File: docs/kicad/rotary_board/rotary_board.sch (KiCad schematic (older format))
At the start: 8 parts

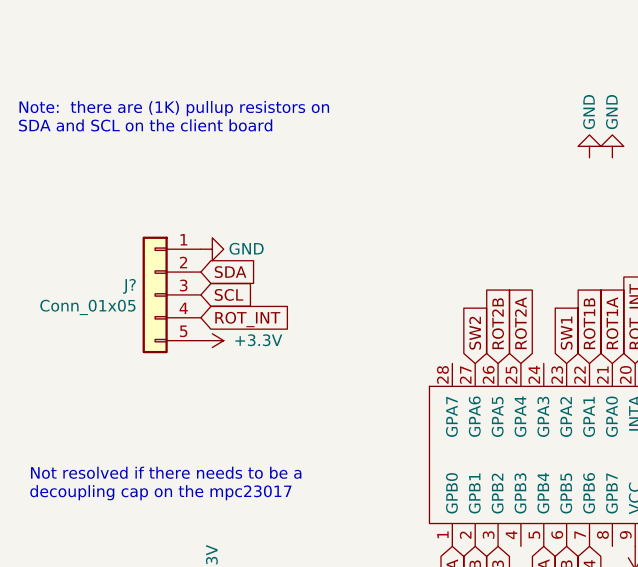
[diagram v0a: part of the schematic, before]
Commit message: got rid of (many) vestigial TE3 design attempts; consolidating electronics under TE3/docs/kicad
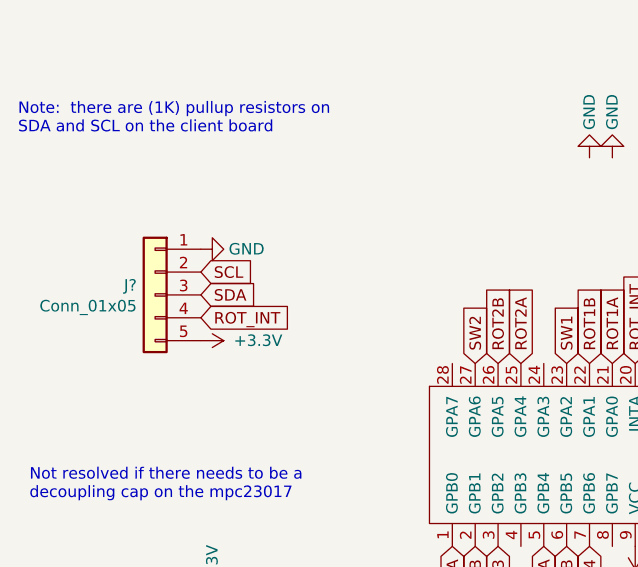
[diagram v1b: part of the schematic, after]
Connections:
- net SCL: now also J?.2 (Pin_2); no longer J?.3 (Pin_3)
- net SDA: now also J?.3 (Pin_3); no longer J?.2 (Pin_2)
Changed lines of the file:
@@
 Text GLabel 5050 3100 3    50   Input ~ 0
 SDA
+Text GLabel 2750 1900 2    50   Input ~ 0
+SCL
 Text GLabel 2750 2000 2    50   Input ~ 0
-SCL
-Text GLabel 2750 1900 2    50   Input ~ 0
 SDA
 Text GLabel 4650 2300 1    50   Input ~ 0

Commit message: tested prototype rotary board
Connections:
- net GND: now also U?.24 (GPA3), U?.28 (GPA7), U?.4 (GPB3), U?.8 (GPB7)
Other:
- note added: "Note: there are (1K) pullup resistors on\nSDA and SCL on the mother_board"
- note removed: "Note: there are (1K) pullup resistors on\nSDA and SCL on the client board"
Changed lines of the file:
@@
 L Device:C C?
 U 1 1 6643CD42
-P 2800 3600
-F 0 "C?" H 2915 3646 50  0001 L CNN
-F 1 "100nf" H 2915 3600 50  0000 L CNN
-F 2 "" H 2838 3450 50  0001 C CNN
-F 3 "~" H 2800 3600 50  0001 C CNN
-	1    2800 3600
+P 2650 3600
+F 0 "C?" H 2765 3646 50  0001 L CNN
+F 1 "100nf" H 2765 3600 50  0000 L CNN
+F 2 "" H 2688 3450 50  0001 C CNN
+F 3 "~" H 2650 3600 50  0001 C CNN
+	1    2650 3600
 	1    0    0    -1
 $EndComp
@@
 L power:+3.3V #PWR?
 U 1 1 66443A19
-P 2800 3450
-F 0 "#PWR?" H 2800 3300 50  0001 C CNN
-F 1 "+3.3V" V 2800 3700 50  0000 C CNN
-F 2 "" H 2800 3450 50  0001 C CNN
-F 3 "" H 2800 3450 50  0001 C CNN
-	1    2800 3450
+P 2650 3450
+F 0 "#PWR?" H 2650 3300 50  0001 C CNN
+F 1 "+3.3V" V 2650 3700 50  0000 C CNN
+F 2 "" H 2650 3450 50  0001 C CNN
+F 3 "" H 2650 3450 50  0001 C CNN
+	1    2650 3450
 	1    0    0    -1
 $EndComp
@@
 L power:GND #PWR?
 U 1 1 66444811
-P 2800 3750
-F 0 "#PWR?" H 2800 3500 50  0001 C CNN
-F 1 "GND" V 2800 3550 50  0000 C CNN
-F 2 "" H 2800 3750 50  0001 C CNN
-F 3 "" H 2800 3750 50  0001 C CNN
-	1    2800 3750
+P 2650 3750
+F 0 "#PWR?" H 2650 3500 50  0001 C CNN
+F 1 "GND" V 2650 3550 50  0000 C CNN
+F 2 "" H 2650 3750 50  0001 C CNN
+F 3 "" H 2650 3750 50  0001 C CNN
+	1    2650 3750
 	1    0    0    -1
 $EndComp
@@
 SW4
 $Comp
-L power:GND #PWR?
-U 1 1 66491CF1
-P 4600 3700
-F 0 "#PWR?" H 4600 3450 50  0001 C CNN
-F 1 "GND" V 4600 3500 50  0000 C CNN
-F 2 "" H 4600 3700 50  0001 C CNN
-F 3 "" H 4600 3700 50  0001 C CNN
-	1    4600 3700
-	1    0    0    -1
-$EndComp
-$Comp
-L power:GND #PWR?
-U 1 1 66491F00
-P 4700 3700
-F 0 "#PWR?" H 4700 3450 50  0001 C CNN
-F 1 "GND" V 4700 3500 50  0000 C CNN
-F 2 "" H 4700 3700 50  0001 C CNN
-F 3 "" H 4700 3700 50  0001 C CNN
-	1    4700 3700
-	1    0    0    -1
-$EndComp
-$Comp
-L power:GND #PWR?
-U 1 1 66495A69
-P 4450 1400
-F 0 "#PWR?" H 4450 1150 50  0001 C CNN
-F 1 "GND" V 4450 1200 50  0000 C CNN
-F 2 "" H 4450 1400 50  0001 C CNN
-F 3 "" H 4450 1400 50  0001 C CNN
-	1    4450 1400
-	-1   0    0    1
-$EndComp
-$Comp
-L power:GND #PWR?
-U 1 1 66495DD6
-P 4550 1400
-F 0 "#PWR?" H 4550 1150 50  0001 C CNN
-F 1 "GND" V 4550 1200 50  0000 C CNN
-F 2 "" H 4550 1400 50  0001 C CNN
-F 3 "" H 4550 1400 50  0001 C CNN
-	1    4550 1400
-	-1   0    0    1
-$EndComp
-$Comp
 L 0_my_symbols:mcp23017 U?
 U 1 1 663ECAFA
@@
 NoConn ~ 4750 2300
 Text Notes 1950 1300 0    50   ~ 0
-Note:  there are (1K) pullup resistors on\nSDA and SCL on the client board
+Note:  there are (1K) pullup resistors on\nSDA and SCL on the mother_board
 Text GLabel 4750 2300 1    50   Input ~ 0
 ROT_INT
@@
 Text Notes 5450 950  0    50   ~ 0
 may want 0.1uf ceramic caps tween pins and ground\nfor hardware debouncing
+$Comp
+L power:GND #PWR?
+U 1 1 66491F00
+P 4550 3100
+F 0 "#PWR?" H 4550 2850 50  0001 C CNN
+F 1 "GND" V 4550 2900 50  0000 C CNN
+F 2 "" H 4550 3100 50  0001 C CNN
+F 3 "" H 4550 3100 50  0001 C CNN
+	1    4550 3100
+	1    0    0    -1
+$EndComp
+$Comp
+L power:GND #PWR?
+U 1 1 66491CF1
+P 4150 3100
+F 0 "#PWR?" H 4150 2850 50  0001 C CNN
+F 1 "GND" V 4150 2900 50  0000 C CNN
+F 2 "" H 4150 3100 50  0001 C CNN
+F 3 "" H 4150 3100 50  0001 C CNN
+	1    4150 3100
+	1    0    0    -1
+$EndComp
+$Comp
+L power:GND #PWR?
+U 1 1 66495DD6
+P 4250 2300
+F 0 "#PWR?" H 4250 2050 50  0001 C CNN
+F 1 "GND" V 4250 2100 50  0000 C CNN
+F 2 "" H 4250 2300 50  0001 C CNN
+F 3 "" H 4250 2300 50  0001 C CNN
+	1    4250 2300
+	-1   0    0    1
+$EndComp
+$Comp
+L power:GND #PWR?
+U 1 1 66495A69
+P 3850 2300
+F 0 "#PWR?" H 3850 2050 50  0001 C CNN
+F 1 "GND" V 3850 2100 50  0000 C CNN
+F 2 "" H 3850 2300 50  0001 C CNN
+F 3 "" H 3850 2300 50  0001 C CNN
+	1    3850 2300
+	-1   0    0    1
+$EndComp
 $EndSCHEMATC

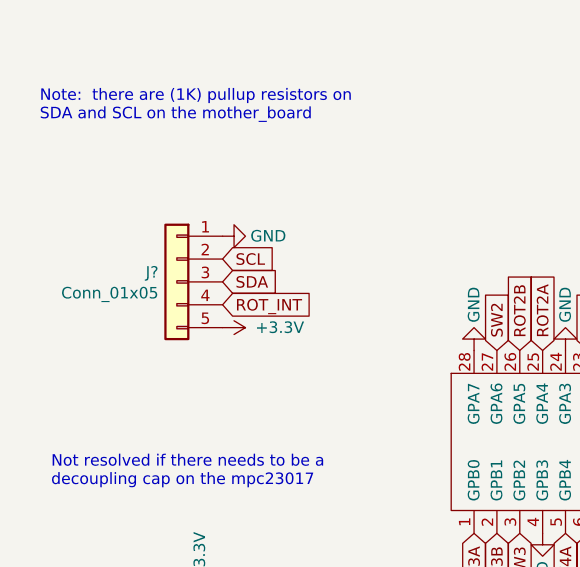
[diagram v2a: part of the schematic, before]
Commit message: kicad changes to support actual Fusion 360 TE3 design efforts - created rotary board PCB
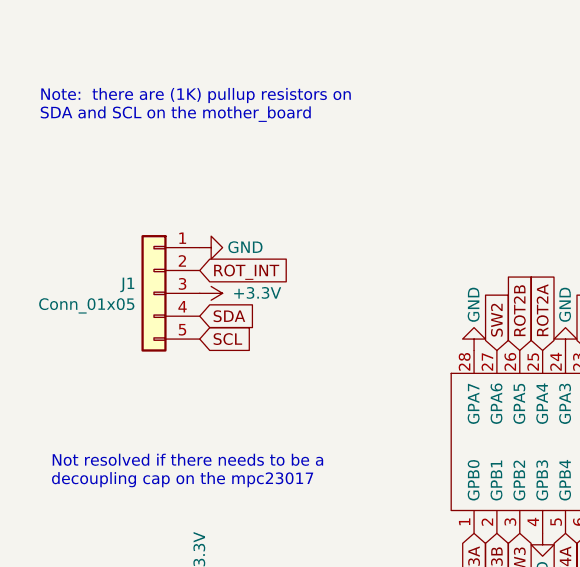
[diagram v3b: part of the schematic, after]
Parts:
- C1: renamed from C?; footprint (none) -> 0_my_footprints:myCapCeramicSmall
- J1: renamed from J?; footprint (none) -> 0_my_footprints:my5Pin
- R1: renamed from R?; footprint (none) -> 0_my_footprints:myResistor
- SW1, SW2, SW3, SW4: renamed from SW?; footprint (none) -> 0_my_footprints:myRotaryEncoder
- U1: renamed from U?; footprint (none) -> 0_my_footprints:myDip28
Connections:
- net +3V3: now also J1.3 (Pin_3); no longer J1.5 (Pin_5)
- net ROT_INT: now also J1.2 (Pin_2); no longer J1.4 (Pin_4)
- net SCL: now also J1.5 (Pin_5); no longer J1.2 (Pin_2)
- net SDA: now also J1.4 (Pin_4); no longer J1.3 (Pin_3)
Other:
- moved on the sheet: J1
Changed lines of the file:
@@
 $EndDescr
 $Comp
-L Device:Rotary_Encoder_Switch SW?
+L Device:Rotary_Encoder_Switch SW1
 U 1 1 663E57E0
 P 6500 1450
-F 0 "SW?" H 6500 1817 50  0001 C CNN
+F 0 "SW1" H 6500 1817 50  0001 C CNN
 F 1 "ROT1" H 6500 1725 50  0000 C CNN
-F 2 "" H 6350 1610 50  0001 C CNN
+F 2 "0_my_footprints:myRotaryEncoder" H 6350 1610 50  0001 C CNN
 F 3 "~" H 6500 1710 50  0001 C CNN
 	1    6500 1450
@@
 $EndComp
 $Comp
-L Connector_Generic:Conn_01x05 J?
+L Connector_Generic:Conn_01x05 J1
 U 1 1 663EE45D
-P 2550 2000
-F 0 "J?" H 2630 2042 50  0000 L CNN
-F 1 "Conn_01x05" H 2630 1951 50  0000 L CNN
-F 2 "" H 2550 2000 50  0001 C CNN
-F 3 "~" H 2550 2000 50  0001 C CNN
-	1    2550 2000
+P 2450 2050
+F 0 "J1" H 2530 2092 50  0000 L CNN
+F 1 "Conn_01x05" H 2530 2001 50  0000 L CNN
+F 2 "0_my_footprints:my5Pin" H 2450 2050 50  0001 C CNN
+F 3 "~" H 2450 2050 50  0001 C CNN
+	1    2450 2050
 	-1   0    0    -1
 $EndComp
 $Comp
-L Device:Rotary_Encoder_Switch SW?
+L Device:Rotary_Encoder_Switch SW2
 U 1 1 663F3D60
 P 6500 2300
-F 0 "SW?" H 6500 2667 50  0001 C CNN
+F 0 "SW2" H 6500 2667 50  0001 C CNN
 F 1 "ROT2" H 6500 2575 50  0000 C CNN
-F 2 "" H 6350 2460 50  0001 C CNN
+F 2 "0_my_footprints:myRotaryEncoder" H 6350 2460 50  0001 C CNN
 F 3 "~" H 6500 2560 50  0001 C CNN
 	1    6500 2300
@@
 $EndComp
 $Comp
-L Device:Rotary_Encoder_Switch SW?
+L Device:Rotary_Encoder_Switch SW3
 U 1 1 663F4490
 P 6500 3150
-F 0 "SW?" H 6500 3517 50  0001 C CNN
+F 0 "SW3" H 6500 3517 50  0001 C CNN
 F 1 "ROT3" H 6500 3425 50  0000 C CNN
-F 2 "" H 6350 3310 50  0001 C CNN
+F 2 "0_my_footprints:myRotaryEncoder" H 6350 3310 50  0001 C CNN
 F 3 "~" H 6500 3410 50  0001 C CNN
 	1    6500 3150
@@
 $EndComp
 $Comp
-L Device:Rotary_Encoder_Switch SW?
+L Device:Rotary_Encoder_Switch SW4
 U 1 1 663F4B46
 P 6500 4050
-F 0 "SW?" H 6500 4417 50  0001 C CNN
+F 0 "SW4" H 6500 4417 50  0001 C CNN
 F 1 "ROT4" H 6500 4325 50  0000 C CNN
-F 2 "" H 6350 4210 50  0001 C CNN
+F 2 "0_my_footprints:myRotaryEncoder" H 6350 4210 50  0001 C CNN
 F 3 "~" H 6500 4310 50  0001 C CNN
 	1    6500 4050
@@
 $EndComp
 $Comp
-L power:GND #PWR?
+L power:GND #PWR03
 U 1 1 663F4E53
-P 2750 1800
-F 0 "#PWR?" H 2750 1550 50  0001 C CNN
-F 1 "GND" V 2750 1600 50  0000 C CNN
-F 2 "" H 2750 1800 50  0001 C CNN
-F 3 "" H 2750 1800 50  0001 C CNN
-	1    2750 1800
-	0    -1   -1   0
-$EndComp
-$Comp
-L power:GND #PWR?
+P 2650 1850
+F 0 "#PWR03" H 2650 1600 50  0001 C CNN
+F 1 "GND" V 2650 1650 50  0000 C CNN
+F 2 "" H 2650 1850 50  0001 C CNN
+F 3 "" H 2650 1850 50  0001 C CNN
+	1    2650 1850
+	0    -1   1    0
+$EndComp
+$Comp
+L power:GND #PWR016
 U 1 1 663F68D2
 P 4750 3100
-F 0 "#PWR?" H 4750 2850 50  0001 C CNN
+F 0 "#PWR016" H 4750 2850 50  0001 C CNN
 F 1 "GND" V 4750 2900 50  0000 C CNN
 F 2 "" H 4750 3100 50  0001 C CNN
@@
 $EndComp
 $Comp
-L power:+3.3V #PWR?
+L power:+3.3V #PWR05
 U 1 1 663F6C65
-P 2750 2200
-F 0 "#PWR?" H 2750 2050 50  0001 C CNN
-F 1 "+3.3V" V 2750 2450 50  0000 C CNN
-F 2 "" H 2750 2200 50  0001 C CNN
-F 3 "" H 2750 2200 50  0001 C CNN
-	1    2750 2200
-	0    1    1    0
+P 2650 2050
+F 0 "#PWR05" H 2650 1900 50  0001 C CNN
+F 1 "+3.3V" V 2650 2300 50  0000 C CNN
+F 2 "" H 2650 2050 50  0001 C CNN
+F 3 "" H 2650 2050 50  0001 C CNN
+	1    2650 2050
+	0    1    -1   0
 $EndComp
 Text GLabel 6800 1350 2    50   Input ~ 0
@@
 ROT4B
 $Comp
-L power:GND #PWR?
+L power:GND #PWR012
 U 1 1 664272DF
 P 6800 2400
-F 0 "#PWR?" H 6800 2150 50  0001 C CNN
+F 0 "#PWR012" H 6800 2150 50  0001 C CNN
 F 1 "GND" V 6800 2200 50  0000 C CNN
 F 2 "" H 6800 2400 50  0001 C CNN
@@
 $EndComp
 $Comp
-L power:GND #PWR?
+L power:GND #PWR020
 U 1 1 66427662
 P 6800 3250
-F 0 "#PWR?" H 6800 3000 50  0001 C CNN
+F 0 "#PWR020" H 6800 3000 50  0001 C CNN
 F 1 "GND" V 6800 3050 50  0000 C CNN
 F 2 "" H 6800 3250 50  0001 C CNN
@@
 $EndComp
 $Comp
-L power:GND #PWR?
+L power:GND #PWR024
 U 1 1 66427948
 P 6800 4150
-F 0 "#PWR?" H 6800 3900 50  0001 C CNN
+F 0 "#PWR024" H 6800 3900 50  0001 C CNN
 F 1 "GND" V 6800 3950 50  0000 C CNN
 F 2 "" H 6800 4150 50  0001 C CNN
@@
 $EndComp
 $Comp
-L power:GND #PWR?
+L power:GND #PWR02
 U 1 1 66428D78
 P 6800 1550
-F 0 "#PWR?" H 6800 1300 50  0001 C CNN
+F 0 "#PWR02" H 6800 1300 50  0001 C CNN
 F 1 "GND" V 6800 1350 50  0000 C CNN
 F 2 "" H 6800 1550 50  0001 C CNN
@@
 $EndComp
 $Comp
-L power:GND #PWR?
+L power:GND #PWR01
 U 1 1 66429552
 P 6200 1450
-F 0 "#PWR?" H 6200 1200 50  0001 C CNN
+F 0 "#PWR01" H 6200 1200 50  0001 C CNN
 F 1 "GND" V 6200 1250 50  0000 C CNN
 F 2 "" H 6200 1450 50  0001 C CNN
@@
 $EndComp
 $Comp
-L power:GND #PWR?
+L power:GND #PWR011
 U 1 1 66429883
 P 6200 2300
-F 0 "#PWR?" H 6200 2050 50  0001 C CNN
+F 0 "#PWR011" H 6200 2050 50  0001 C CNN
 F 1 "GND" V 6200 2100 50  0000 C CNN
 F 2 "" H 6200 2300 50  0001 C CNN
@@
 $EndComp
 $Comp
-L power:GND #PWR?
+L power:GND #PWR019
 U 1 1 6642A07A
 P 6200 3150
-F 0 "#PWR?" H 6200 2900 50  0001 C CNN
+F 0 "#PWR019" H 6200 2900 50  0001 C CNN
 F 1 "GND" V 6200 2950 50  0000 C CNN
 F 2 "" H 6200 3150 50  0001 C CNN
@@
 $EndComp
 $Comp
-L power:GND #PWR?
+L power:GND #PWR023
 U 1 1 6642A3A3
 P 6200 4050
-F 0 "#PWR?" H 6200 3800 50  0001 C CNN
+F 0 "#PWR023" H 6200 3800 50  0001 C CNN
 F 1 "GND" V 6200 3850 50  0000 C CNN
 F 2 "" H 6200 4050 50  0001 C CNN
@@
 $EndComp
 $Comp
-L power:+3.3V #PWR?
+L power:+3.3V #PWR015
 U 1 1 6643C635
 P 4650 3100
-F 0 "#PWR?" H 4650 2950 50  0001 C CNN
+F 0 "#PWR015" H 4650 2950 50  0001 C CNN
 F 1 "+3.3V" V 4650 3350 50  0000 C CNN
 F 2 "" H 4650 3100 50  0001 C CNN
@@
 $EndComp
 $Comp
-L Device:R R?
+L Device:R R1
 U 1 1 6643CB12
 P 4850 2050
-F 0 "R?" H 4920 2096 50  0001 L CNN
+F 0 "R1" H 4920 2096 50  0001 L CNN
 F 1 "10K" V 4850 2050 50  0000 C CNN
-F 2 "" V 4780 2050 50  0001 C CNN
+F 2 "0_my_footprints:myResistor" V 4780 2050 50  0001 C CNN
 F 3 "~" H 4850 2050 50  0001 C CNN
 	1    4850 2050
@@
 $EndComp
 $Comp
-L Device:C C?
+L Device:C C1
 U 1 1 6643CD42
 P 2650 3600
-F 0 "C?" H 2765 3646 50  0001 L CNN
+F 0 "C1" H 2765 3646 50  0001 L CNN
 F 1 "100nf" H 2765 3600 50  0000 L CNN
-F 2 "" H 2688 3450 50  0001 C CNN
+F 2 "0_my_footprints:myCapCeramicSmall" H 2688 3450 50  0001 C CNN
 F 3 "~" H 2650 3600 50  0001 C CNN
 	1    2650 3600
@@
 $EndComp
 $Comp
-L power:+3.3V #PWR?
+L power:+3.3V #PWR021
 U 1 1 66443A19
 P 2650 3450
-F 0 "#PWR?" H 2650 3300 50  0001 C CNN
+F 0 "#PWR021" H 2650 3300 50  0001 C CNN
 F 1 "+3.3V" V 2650 3700 50  0000 C CNN
 F 2 "" H 2650 3450 50  0001 C CNN
@@
 $EndComp
 $Comp
-L power:GND #PWR?
+L power:GND #PWR022
 U 1 1 66444811
 P 2650 3750
-F 0 "#PWR?" H 2650 3500 50  0001 C CNN
+F 0 "#PWR022" H 2650 3500 50  0001 C CNN
 F 1 "GND" V 2650 3550 50  0000 C CNN
 F 2 "" H 2650 3750 50  0001 C CNN
@@
 $EndComp
 $Comp
-L power:+3.3V #PWR?
+L power:+3.3V #PWR04
 U 1 1 664504D1
 P 4850 1800
-F 0 "#PWR?" H 4850 1650 50  0001 C CNN
+F 0 "#PWR04" H 4850 1650 50  0001 C CNN
 F 1 "+3.3V" V 4850 2050 50  0000 C CNN
 F 2 "" H 4850 1800 50  0001 C CNN
@@
 SW4
 $Comp
-L 0_my_symbols:mcp23017 U?
+L 0_my_symbols:mcp23017 U1
 U 1 1 663ECAFA
 P 4500 2700
-F 0 "U?" H 5228 2746 50  0001 L CNN
+F 0 "U1" H 5228 2746 50  0001 L CNN
 F 1 "mcp23017" H 4700 2700 50  0000 L CNN
-F 2 "" H 4750 2450 50  0001 C CNN
+F 2 "0_my_footprints:myDip28" H 4750 2450 50  0001 C CNN
 F 3 "" H 4750 2450 50  0001 C CNN
 	1    4500 2700
@@
 $EndComp
 $Comp
-L power:GND #PWR?
+L power:GND #PWR010
 U 1 1 66499F8B
 P 5150 2300
-F 0 "#PWR?" H 5150 2050 50  0001 C CNN
+F 0 "#PWR010" H 5150 2050 50  0001 C CNN
 F 1 "GND" V 5150 2100 50  0000 C CNN
 F 2 "" H 5150 2300 50  0001 C CNN
@@
 $EndComp
 $Comp
-L power:GND #PWR?
+L power:GND #PWR09
 U 1 1 6649A25F
 P 5050 2300
-F 0 "#PWR?" H 5050 2050 50  0001 C CNN
+F 0 "#PWR09" H 5050 2050 50  0001 C CNN
 F 1 "GND" V 5050 2100 50  0000 C CNN
 F 2 "" H 5050 2300 50  0001 C CNN
@@
 $EndComp
 $Comp
-L power:GND #PWR?
+L power:GND #PWR08
 U 1 1 6649A57A
 P 4950 2300
-F 0 "#PWR?" H 4950 2050 50  0001 C CNN
+F 0 "#PWR08" H 4950 2050 50  0001 C CNN
 F 1 "GND" V 4950 2100 50  0000 C CNN
 F 2 "" H 4950 2300 50  0001 C CNN
@@
 $EndComp
 $Comp
-L power:GND #PWR?
+L power:GND #PWR017
 U 1 1 6649A95A
 P 4850 3100
-F 0 "#PWR?" H 4850 2850 50  0001 C CNN
+F 0 "#PWR017" H 4850 2850 50  0001 C CNN
 F 1 "GND" V 4850 2900 50  0000 C CNN
 F 2 "" H 4850 3100 50  0001 C CNN
@@
 $EndComp
 $Comp
-L power:GND #PWR?
+L power:GND #PWR018
 U 1 1 6649AD0A
 P 5150 3100
-F 0 "#PWR?" H 5150 2850 50  0001 C CNN
+F 0 "#PWR018" H 5150 2850 50  0001 C CNN
 F 1 "GND" V 5150 2900 50  0000 C CNN
 F 2 "" H 5150 3100 50  0001 C CNN
@@
 Text GLabel 5050 3100 3    50   Input ~ 0
 SDA
-Text GLabel 2750 1900 2    50   Input ~ 0
+Text GLabel 2650 2250 2    50   Input ~ 0
 SCL
-Text GLabel 2750 2000 2    50   Input ~ 0
+Text GLabel 2650 2150 2    50   Input ~ 0
 SDA
 Text GLabel 4650 2300 1    50   Input ~ 0
 ROT_INT
-Text GLabel 2750 2100 2    50   Input ~ 0
+Text GLabel 2650 1950 2    50   Input ~ 0
 ROT_INT
 NoConn ~ 4750 2300
@@
 may want 0.1uf ceramic caps tween pins and ground\nfor hardware debouncing
 $Comp
-L power:GND #PWR?
+L power:GND #PWR014
 U 1 1 66491F00
 P 4550 3100
-F 0 "#PWR?" H 4550 2850 50  0001 C CNN
+F 0 "#PWR014" H 4550 2850 50  0001 C CNN
 F 1 "GND" V 4550 2900 50  0000 C CNN
 F 2 "" H 4550 3100 50  0001 C CNN
@@
 $EndComp
 $Comp
-L power:GND #PWR?
+L power:GND #PWR013
 U 1 1 66491CF1
 P 4150 3100
-F 0 "#PWR?" H 4150 2850 50  0001 C CNN
+F 0 "#PWR013" H 4150 2850 50  0001 C CNN
 F 1 "GND" V 4150 2900 50  0000 C CNN
 F 2 "" H 4150 3100 50  0001 C CNN
@@
 $EndComp
 $Comp
-L power:GND #PWR?
+L power:GND #PWR07
 U 1 1 66495DD6
 P 4250 2300
-F 0 "#PWR?" H 4250 2050 50  0001 C CNN
+F 0 "#PWR07" H 4250 2050 50  0001 C CNN
 F 1 "GND" V 4250 2100 50  0000 C CNN
 F 2 "" H 4250 2300 50  0001 C CNN
@@
 $EndComp
 $Comp
-L power:GND #PWR?
+L power:GND #PWR06
 U 1 1 66495A69
 P 3850 2300
-F 0 "#PWR?" H 3850 2050 50  0001 C CNN
+F 0 "#PWR06" H 3850 2050 50  0001 C CNN
 F 1 "GND" V 3850 2100 50  0000 C CNN
 F 2 "" H 3850 2300 50  0001 C CNN
